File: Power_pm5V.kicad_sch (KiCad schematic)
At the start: 36 parts, among them IC15 LT3090EMSE#PBF, IC16 LT3085EMS8E#TRPBF, J25 Conn_01x04, J27 Conn_Coaxial, J28 Conn_Coaxial

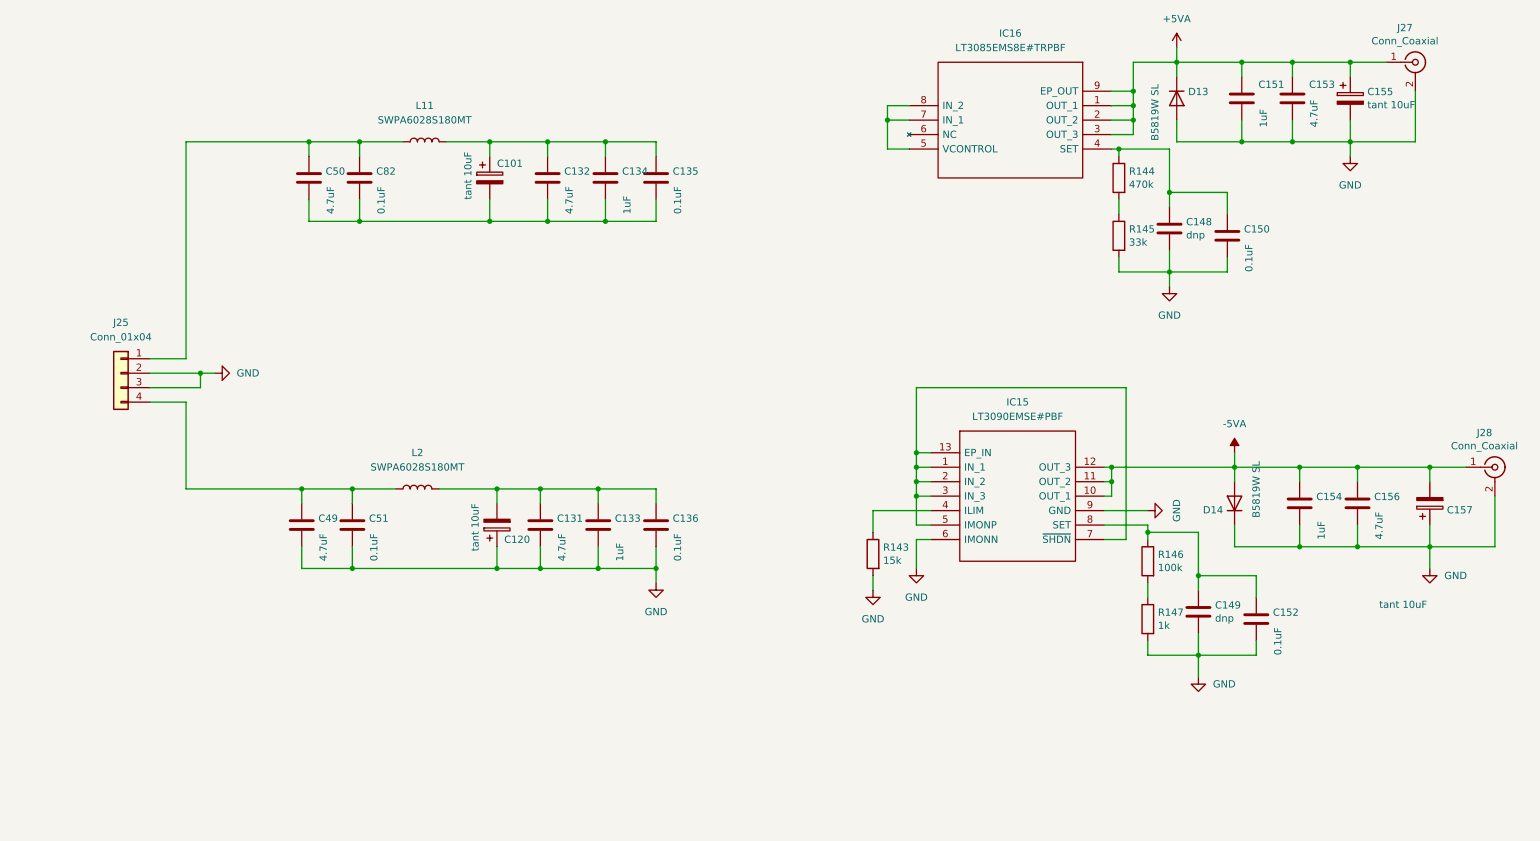
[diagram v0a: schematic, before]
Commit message: Preliminary layout of analog portions
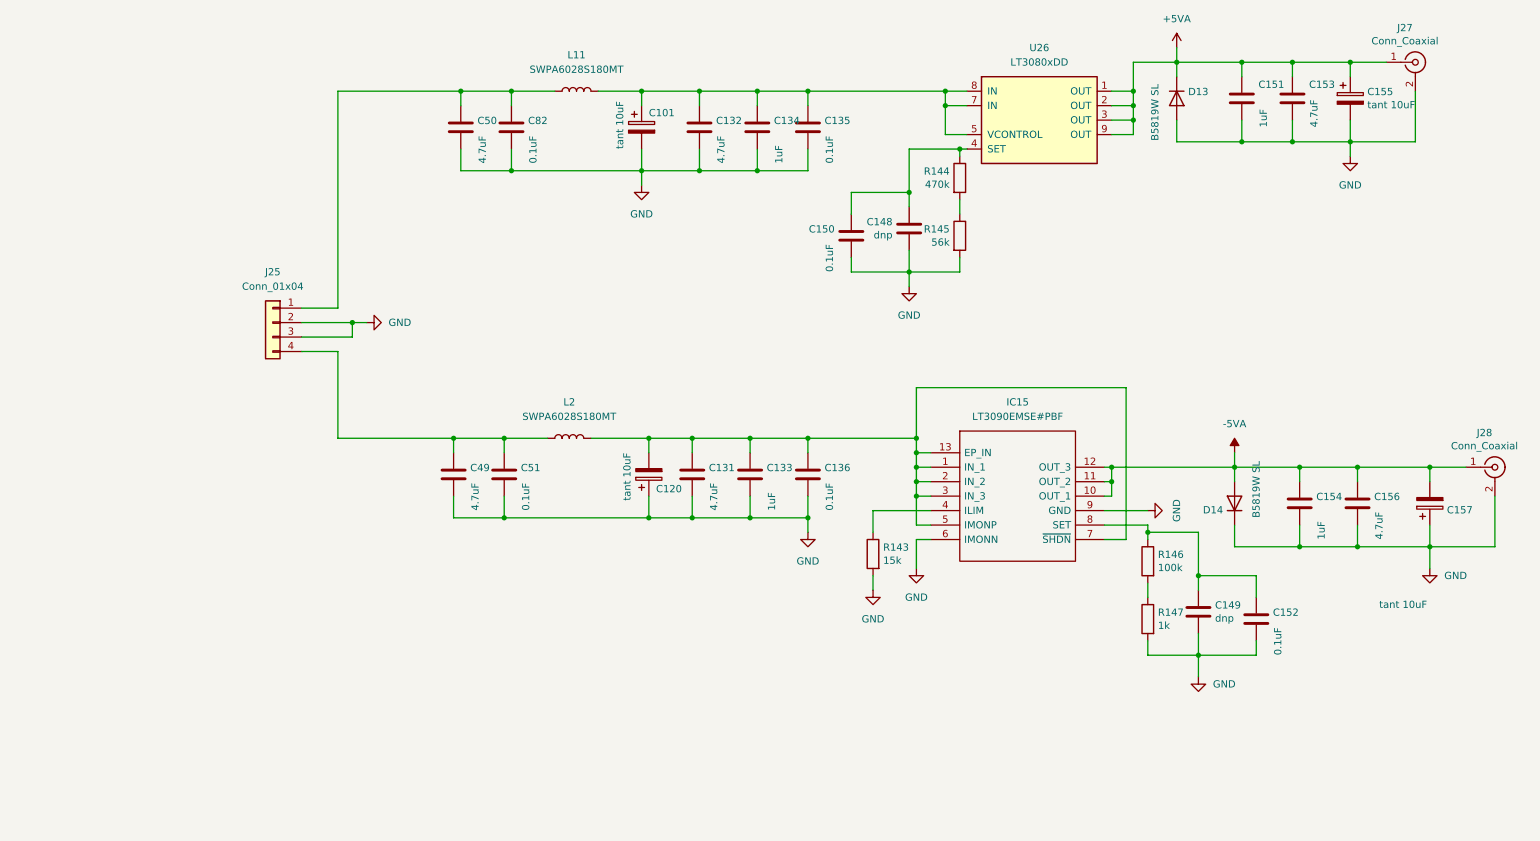
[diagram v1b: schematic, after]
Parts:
- removed IC16: LT3085EMS8E#TRPBF, SamacSys_Parts:SOP65P490X110-9N, symbol HanzhenCustomLib:LT3085EMS8E#TRPBF
- added U26: LT3080xDD, Package_DFN_QFN:DFN-8-1EP_3x3mm_P0.5mm_EP1.66x2.38mm, symbol Regulator_Linear:LT3080xDD
- R145: value 33k -> 56k
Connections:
- net +5VA: now also U26.1 (OUT), U26.2 (OUT), U26.3 (OUT), U26.9 (OUT)
- net GND: now also C101.2, C132.2, C134.2, C135.2, C50.2, C82.2
- net at C120.2, C131.1, C133.1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: now also IC15.1 (IN_1), IC15.13 (EP_IN), IC15.2 (IN_2), IC15.3 (IN_3), IC15.5 (IMONP), IC15.7 (~{SHDN})
- net at C101.1, C132.1, C134.1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: now also U26.5 (VCONTROL), U26.7 (IN), U26.8 (IN)
- net at C148.1, C150.1, R144.1: now also U26.4 (SET)
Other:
- moved on the sheet: C101, C120, C131, C132, C133, C134, C135, C136, C148, C150, C49, C50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

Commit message: First finished draft
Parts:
- added C174, C175: OVK101M1ETR-0608, Capacitor_SMD:CP_Elec_6.3x7.7, symbol Device:C_Polarized
- C101, C120, C155, C157: symbol Device:CP -> Device:C_Polarized
- R147: value 1k -> 4k7
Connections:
- net +5VA: now also C174.1
- net -5VA: now also C175.2
- net GND: now also C174.2, C175.1
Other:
- moved on the sheet: C101, C120, C131, C132, C133, C134, C135, C136, C148, C149, C150, C151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

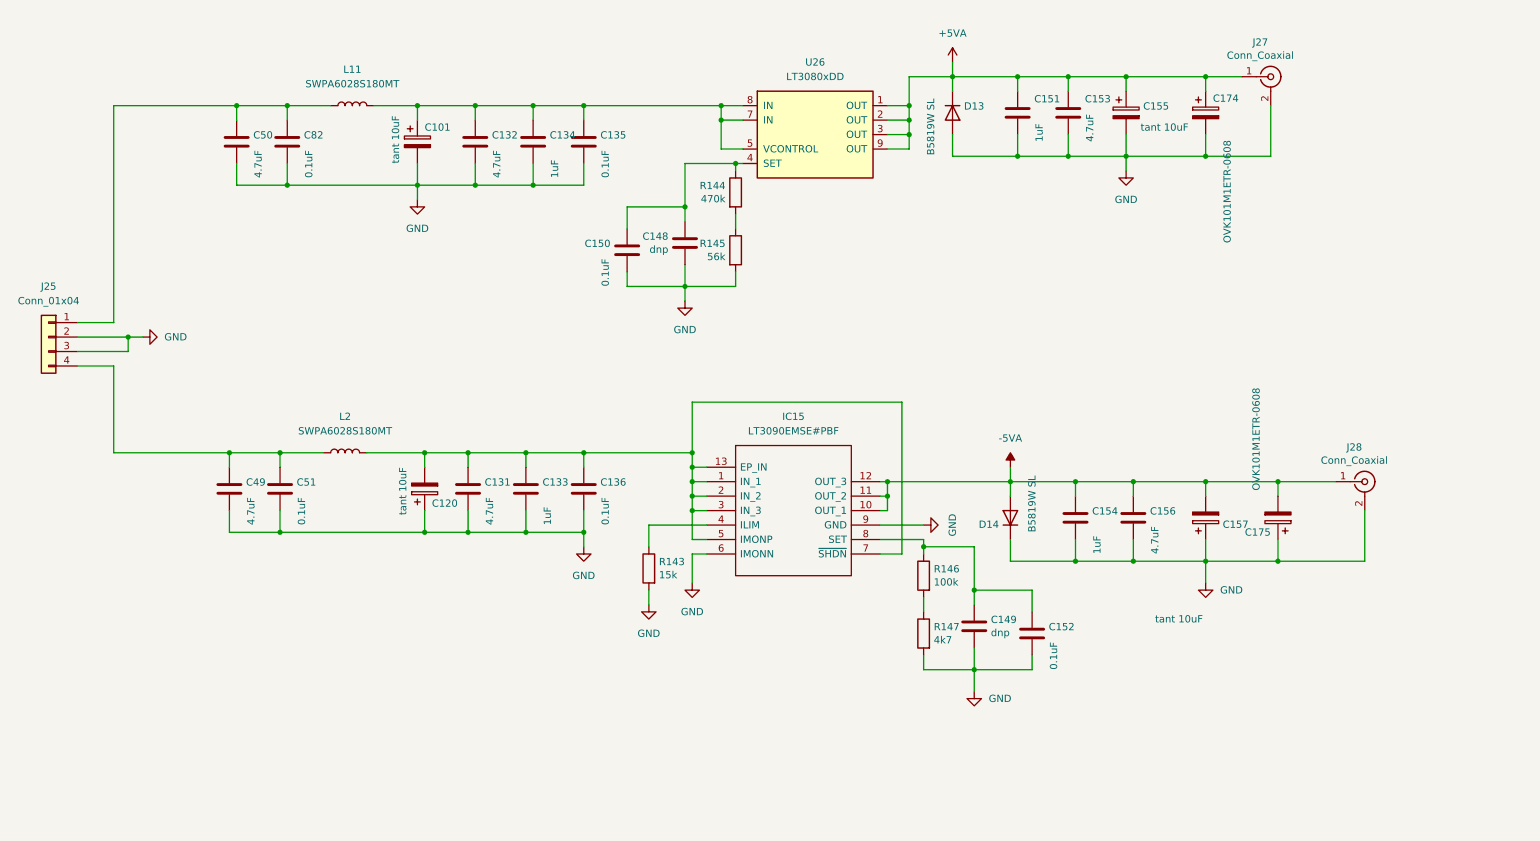
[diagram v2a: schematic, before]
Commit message: Version 1.0 submitted to JLCPCB
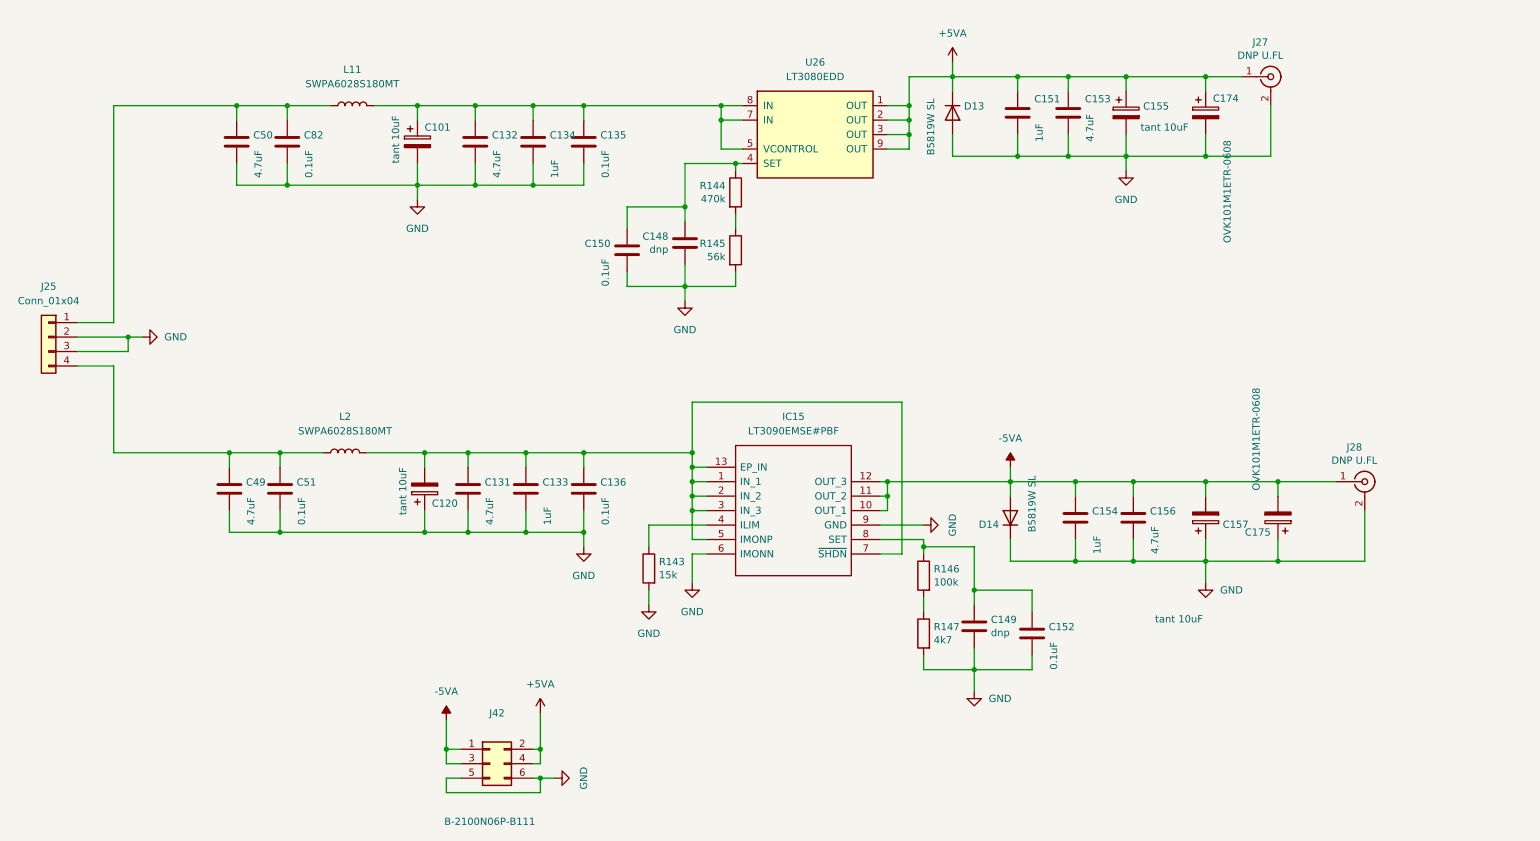
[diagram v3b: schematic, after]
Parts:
- added J42: B-2100N06P-B111, Connector_PinHeader_2.54mm:PinHeader_2x03_P2.54mm_Vertical_SMD, symbol Connector_Generic:Conn_02x03_Odd_Even
- D13, D14: footprint Diode_SMD:D_SOD-123F -> Diode_SMD:D_SOD-123
- J27, J28: value Conn_Coaxial -> DNP U.FL
- U26: value LT3080xDD -> LT3080EDD
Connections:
- net +5VA: now also J42.2 (Pin_2), J42.4 (Pin_4)
- net -5VA: now also J42.1 (Pin_1), J42.3 (Pin_3)
- net GND: now also J42.5 (Pin_5), J42.6 (Pin_6)
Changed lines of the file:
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@@
 (kicad_sch (version 20211123) (generator eeschema)
   (paper "A4")
+  (junction (at 106.68 153.67) (diameter 0) (color 0 0 0 0)
+  )
   (junction (at 133.35 101.6) (diameter 0) (color 0 0 0 0)
   )
@@
   (junction (at 132.08 72.39) (diameter 0) (color 0 0 0 0)
   )
+  (junction (at 90.17 153.67) (diameter 0) (color 0 0 0 0)
+  )
   (junction (at 199.39 49.53) (diameter 0) (color 0 0 0 0)
   )
@@
   (junction (at 133.35 106.68) (diameter 0) (color 0 0 0 0)
   )
+  (junction (at 106.68 158.75) (diameter 0) (color 0 0 0 0)
+  )
   (junction (at 173.99 118.11) (diameter 0) (color 0 0 0 0)
   )
@@
     (stroke (width 0) (type default) (color 0 0 0 0))
   )
+  (wire (pts (xy 106.68 147.32) (xy 106.68 153.67))
+    (stroke (width 0) (type default) (color 0 0 0 0))
+  )
   (wire (pts (xy 179.07 49.53) (xy 190.5 49.53))
     (stroke (width 0) (type default) (color 0 0 0 0))
@@
     (stroke (width 0) (type default) (color 0 0 0 0))
   )
+  (wire (pts (xy 92.71 156.21) (xy 90.17 156.21))
+    (stroke (width 0) (type default) (color 0 0 0 0))
+  )
   (wire (pts (xy 182.88 135.89) (xy 182.88 139.7))
     (stroke (width 0) (type default) (color 0 0 0 0))
@@
     (stroke (width 0) (type default) (color 0 0 0 0))
   )
+  (wire (pts (xy 105.41 158.75) (xy 106.68 158.75))
+    (stroke (width 0) (type default) (color 0 0 0 0))
+  )
+  (wire (pts (xy 106.68 153.67) (xy 106.68 156.21))
+    (stroke (width 0) (type default) (color 0 0 0 0))
+  )
   (wire (pts (xy 189.23 106.68) (xy 200.66 106.68))
     (stroke (width 0) (type default) (color 0 0 0 0))
@@
     (stroke (width 0) (type default) (color 0 0 0 0))
   )
+  (wire (pts (xy 90.17 161.29) (xy 90.17 158.75))
+    (stroke (width 0) (type default) (color 0 0 0 0))
+  )
   (wire (pts (xy 200.66 106.68) (xy 200.66 109.22))
     (stroke (width 0) (type default) (color 0 0 0 0))
@@
     (stroke (width 0) (type default) (color 0 0 0 0))
   )
+  (wire (pts (xy 106.68 161.29) (xy 90.17 161.29))
+    (stroke (width 0) (type default) (color 0 0 0 0))
+  )
   (wire (pts (xy 31.75 101.6) (xy 52.07 101.6))
     (stroke (width 0) (type default) (color 0 0 0 0))
@@
     (stroke (width 0) (type default) (color 0 0 0 0))
   )
+  (wire (pts (xy 106.68 158.75) (xy 109.22 158.75))
+    (stroke (width 0) (type default) (color 0 0 0 0))
+  )
   (wire (pts (xy 190.5 35.56) (xy 199.39 35.56))
     (stroke (width 0) (type default) (color 0 0 0 0))
@@
     (stroke (width 0) (type default) (color 0 0 0 0))
   )
+  (wire (pts (xy 105.41 153.67) (xy 106.68 153.67))
+    (stroke (width 0) (type default) (color 0 0 0 0))
+  )
   (wire (pts (xy 62.23 40.64) (xy 62.23 43.18))
     (stroke (width 0) (type default) (color 0 0 0 0))
@@
     (stroke (width 0) (type default) (color 0 0 0 0))
   )
+  (wire (pts (xy 106.68 156.21) (xy 105.41 156.21))
+    (stroke (width 0) (type default) (color 0 0 0 0))
+  )
   (wire (pts (xy 125.73 114.3) (xy 135.89 114.3))
     (stroke (width 0) (type default) (color 0 0 0 0))
@@
     (stroke (width 0) (type default) (color 0 0 0 0))
   )
+  (wire (pts (xy 90.17 148.59) (xy 90.17 153.67))
+    (stroke (width 0) (type default) (color 0 0 0 0))
+  )
   (wire (pts (xy 85.09 40.64) (xy 95.25 40.64))
     (stroke (width 0) (type default) (color 0 0 0 0))
@@
     (stroke (width 0) (type default) (color 0 0 0 0))
   )
+  (wire (pts (xy 106.68 158.75) (xy 106.68 161.29))
+    (stroke (width 0) (type default) (color 0 0 0 0))
+  )
   (wire (pts (xy 236.22 109.22) (xy 236.22 106.68))
     (stroke (width 0) (type default) (color 0 0 0 0))
@@
     (stroke (width 0) (type default) (color 0 0 0 0))
   )
+  (wire (pts (xy 90.17 156.21) (xy 90.17 153.67))
+    (stroke (width 0) (type default) (color 0 0 0 0))
+  )
   (wire (pts (xy 133.35 101.6) (xy 133.35 104.14))
     (stroke (width 0) (type default) (color 0 0 0 0))
@@
   )
   (wire (pts (xy 60.96 101.6) (xy 68.58 101.6))
+    (stroke (width 0) (type default) (color 0 0 0 0))
+  )
+  (wire (pts (xy 90.17 158.75) (xy 92.71 158.75))
+    (stroke (width 0) (type default) (color 0 0 0 0))
+  )
+  (wire (pts (xy 90.17 153.67) (xy 92.71 153.67))
     (stroke (width 0) (type default) (color 0 0 0 0))
   )
@@
     (pin "2")
   )
+  (symbol (lib_id "power:-5VA") (at 90.17 148.59 0) (unit 1)
+    (in_bom yes) (on_board yes) (fields_autoplaced)
+    (property "Reference" "#PWR0248" (id 0) (at 90.17 146.05 0)
+      (effects (font (size 1.27 1.27)) hide)
+    )
+    (property "Value" "-5VA" (id 1) (at 90.17 143.51 0))
+    (property "Footprint" "" (id 2) (at 90.17 148.59 0)
+      (effects (font (size 1.27 1.27)) hide)
+    )
+    (property "Datasheet" "" (id 3) (at 90.17 148.59 0)
+      (effects (font (size 1.27 1.27)) hide)
+    )
+    (pin "1")
+  )
   (symbol (lib_id "power:+5VA") (at 179.07 33.02 0) (unit 1)
     (in_bom yes) (on_board yes) (fields_autoplaced)
@@
       (effects (font (size 1.27 1.27)) (justify left))
     )
-    (property "Footprint" "Diode_SMD:D_SOD-123F" (id 2) (at 179.07 41.91 0)
+    (property "Footprint" "Diode_SMD:D_SOD-123" (id 2) (at 179.07 41.91 0)
       (effects (font (size 1.27 1.27)) hide)
     )
@@
     (in_bom yes) (on_board yes) (fields_autoplaced)
     (property "Reference" "U26" (id 0) (at 154.94 33.02 0))
-    (property "Value" "LT3080xDD" (id 1) (at 154.94 35.56 0))
+    (property "Value" "LT3080EDD" (id 1) (at 154.94 35.56 0))
     (property "Footprint" "Package_DFN_QFN:DFN-8-1EP_3x3mm_P0.5mm_EP1.66x2.38mm" (id 2) (at 154.94 55.88 0)
       (effects (font (size 1.27 1.27)) hide)
@@
     (in_bom yes) (on_board yes)
     (property "Reference" "J27" (id 0) (at 233.1212 29.5148 0))
-    (property "Value" "Conn_Coaxial" (id 1) (at 233.1212 31.8262 0))
+    (property "Value" "DNP U.FL" (id 1) (at 233.1212 31.8262 0))
     (property "Footprint" "Connector_Coaxial:U.FL_Hirose_U.FL-R-SMT-1_Vertical" (id 2) (at 234.95 35.56 0)
       (effects (font (size 1.27 1.27)) hide)
@@
     (in_bom yes) (on_board yes)
     (property "Reference" "J28" (id 0) (at 249.6312 100.6348 0))
-    (property "Value" "Conn_Coaxial" (id 1) (at 249.6312 102.9462 0))
+    (property "Value" "DNP U.FL" (id 1) (at 249.6312 102.9462 0))
     (property "Footprint" "Connector_Coaxial:U.FL_Hirose_U.FL-R-SMT-1_Vertical" (id 2) (at 251.46 106.68 0)
       (effects (font (size 1.27 1.27)) hide)
@@
     (pin "4")
   )
+  (symbol (lib_id "power:GND") (at 109.22 158.75 90) (unit 1)
+    (in_bom yes) (on_board yes) (fields_autoplaced)
+    (property "Reference" "#PWR0291" (id 0) (at 115.57 158.75 0)
+      (effects (font (size 1.27 1.27)) hide)
+    )
+    (property "Value" "GND" (id 1) (at 114.3 158.75 0))
+    (property "Footprint" "" (id 2) (at 109.22 158.75 0)
+      (effects (font (size 1.27 1.27)) hide)
+    )
+    (property "Datasheet" "" (id 3) (at 109.22 158.75 0)
+      (effects (font (size 1.27 1.27)) hide)
+    )
+    (pin "1")
+  )
+  (symbol (lib_id "Connector_Generic:Conn_02x03_Odd_Even") (at 97.79 156.21 0) (unit 1)
+    (in_bom yes) (on_board yes)
+    (property "Reference" "J42" (id 0) (at 99.06 147.32 0))
+    (property "Value" "B-2100N06P-B111" (id 1) (at 97.79 166.37 0))
+    (property "Footprint" "Connector_PinHeader_2.54mm:PinHeader_2x03_P2.54mm_Vertical_SMD" (id 2) (at 97.79 156.21 0)
+      (effects (font (size 1.27 1.27)) hide)
+    )
+    (property "Datasheet" "~" (id 3) (at 97.79 156.21 0)
+      (effects (font (size 1.27 1.27)) hide)
+    )
+    (pin "1")
+    (pin "2")
+    (pin "3")
+    (pin "4")
+    (pin "5")
+    (pin "6")
+  )
   (symbol (lib_id "Device:C") (at 199.39 41.91 0) (unit 1)
     (in_bom yes) (on_board yes)
@@
     (pin "2")
   )
+  (symbol (lib_id "power:+5VA") (at 106.68 147.32 0) (unit 1)
+    (in_bom yes) (on_board yes) (fields_autoplaced)
+    (property "Reference" "#PWR0290" (id 0) (at 106.68 151.13 0)
+      (effects (font (size 1.27 1.27)) hide)
+    )
+    (property "Value" "+5VA" (id 1) (at 106.68 142.24 0))
+    (property "Footprint" "" (id 2) (at 106.68 147.32 0)
+      (effects (font (size 1.27 1.27)) hide)
+    )
+    (property "Datasheet" "" (id 3) (at 106.68 147.32 0)
+      (effects (font (size 1.27 1.27)) hide)
+    )
+    (pin "1")
+  )
   (symbol (lib_id "Device:D") (at 189.23 113.03 90) (unit 1)
     (in_bom yes) (on_board yes)
@@
       (effects (font (size 1.27 1.27)) (justify left))
     )
-    (property "Footprint" "Diode_SMD:D_SOD-123F" (id 2) (at 189.23 113.03 0)
-      (effects (font (size 1.27 1.27)) hide)
-    )
+    (property "Footprint" "Diode_SMD:D_SOD-123" (id 2) (at 189.23 113.03 0)
+      (effects (font (size 1.27 1.27)) hide)
+    )
